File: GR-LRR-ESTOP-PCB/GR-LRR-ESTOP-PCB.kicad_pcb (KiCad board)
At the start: 2 copper layers, 35 x 70 mm, 0 parts

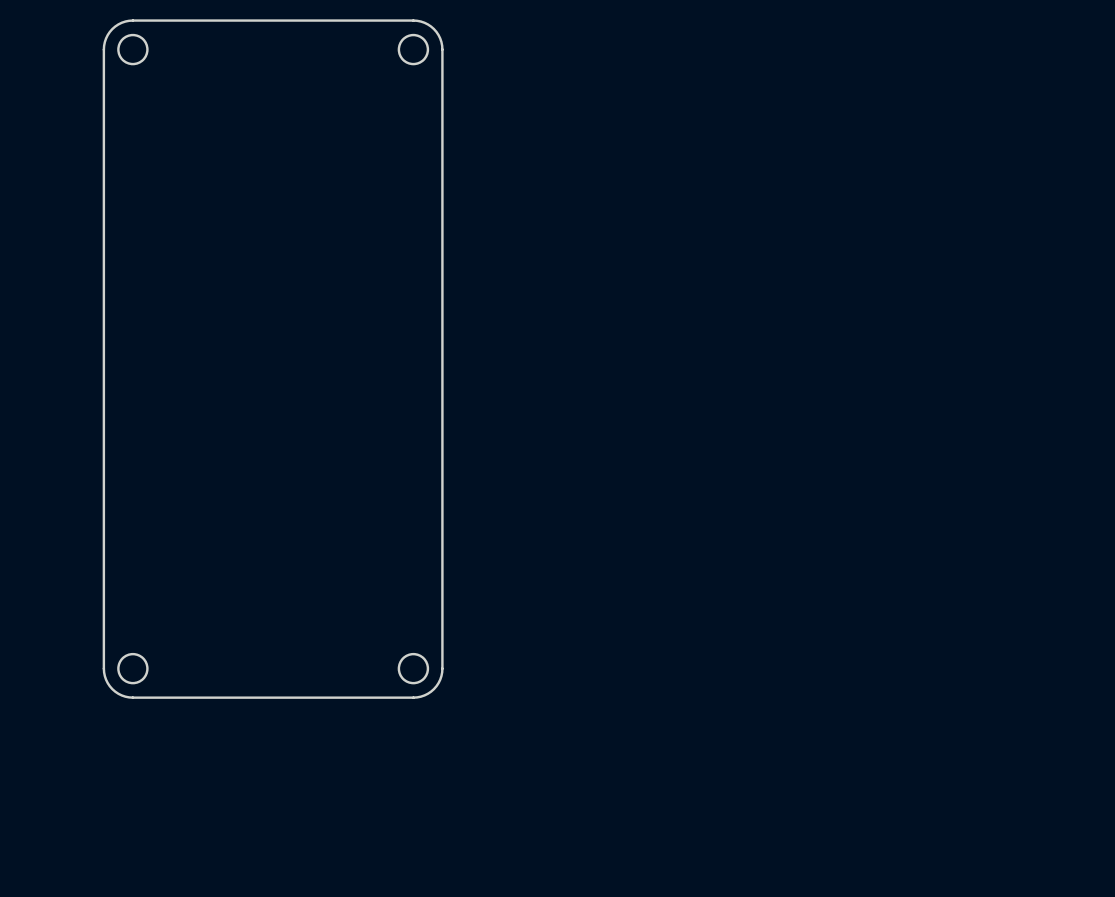
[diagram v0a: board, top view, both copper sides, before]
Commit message: moving to two enclosures
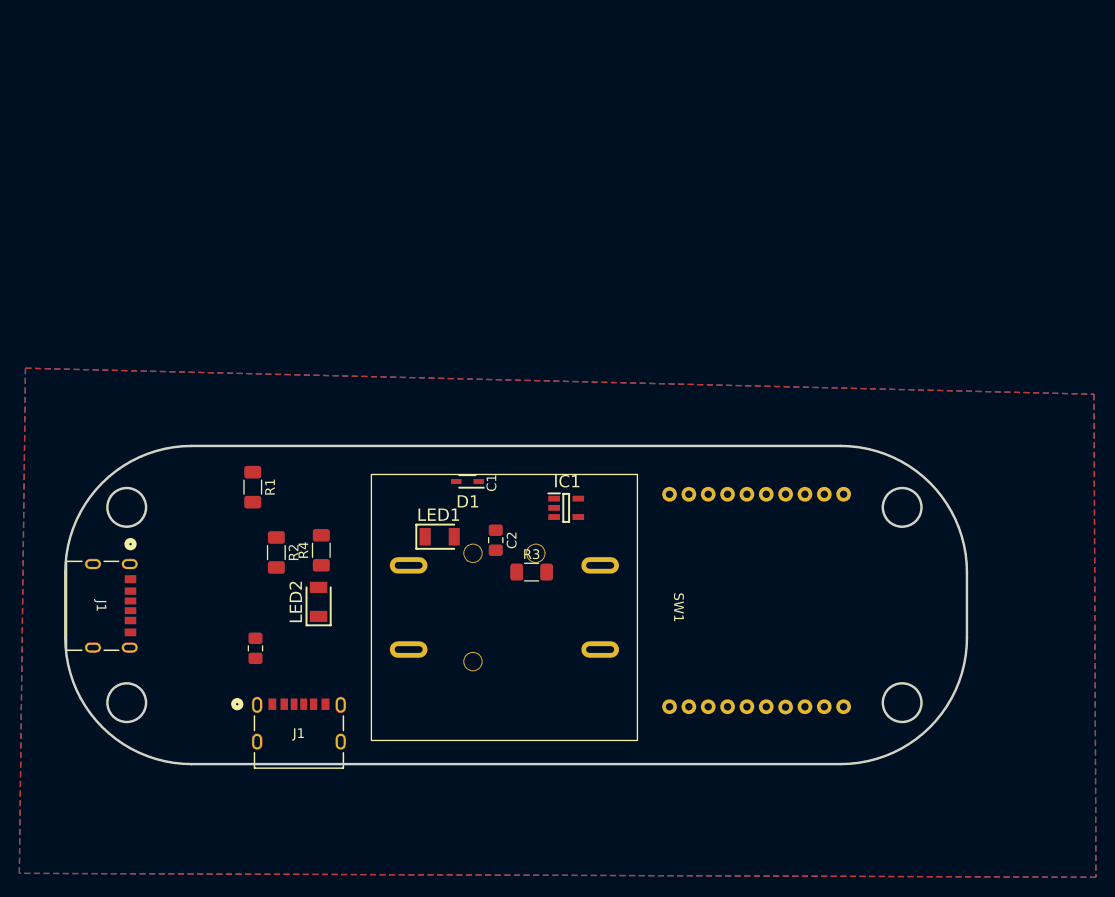
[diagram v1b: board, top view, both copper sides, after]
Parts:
- added C1: 1uF, 10V, Capacitor_SMD:C_0805_2012Metric_Pad1.18x1.45mm_HandSolder, F.Cu at (88.2, 127.7)
- added C2: 1uF, 10V, Capacitor_SMD:C_0805_2012Metric_Pad1.18x1.45mm_HandSolder, F.Cu at (113.0, 116.5)
- added D1: ZLLS400TA, ZLLS400TA:SOD2513X120N, F.Cu at (110.1, 110.4)
- added IC1: TLV75533PDBVR, TLV75533PDBVR:SOT95P280X145-5N, F.Cu at (120.3, 113.2)
- added J1: 10164359-00011LF, 10164359_00011LF:CONN_10164359-00011LF_AMP, F.Cu at (92.7, 136.5)
- added J1: 10164359-00011LF, 10164359_00011LF:CONN_10164359-00011LF_AMP, F.Cu at (72.2, 123.3)
- added LED1: QTLP650C2TR, QTLP650C2TR:LEDC3216X130N, F.Cu at (107.2, 116.1)
- added LED2: QTLP650C2TR, QTLP650C2TR:LEDC3216X130N, F.Cu at (94.7, 122.9)
- added R1: 1k, Resistor_SMD:R_1206_3216Metric_Pad1.30x1.75mm_HandSolder, F.Cu at (87.9, 111.0)
- added R2: 1k, Resistor_SMD:R_1206_3216Metric_Pad1.30x1.75mm_HandSolder, F.Cu at (90.3, 117.8)
- added R3: 86ohm, 1/10w, Resistor_SMD:R_1206_3216Metric_Pad1.30x1.75mm_HandSolder, F.Cu at (116.7, 119.8)
- added R4: 86ohm, 1/10w, Resistor_SMD:R_1206_3216Metric_Pad1.30x1.75mm_HandSolder, F.Cu at (95.0, 117.6)
- added SW1: ~, XA1E-BV302-R:XA1E-BV302-R, F.Cu at (113.9, 123.5)
- added U1: ~, XB3-24AST-J:XB3-24AST-J, B.Cu at (143.0, 122.8)
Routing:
- added copper zone on B.Cu, net GND
- added copper zone on F.Cu, net GND
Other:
- board size 35 x 70 mm -> 93.2 x 32.9 mm
